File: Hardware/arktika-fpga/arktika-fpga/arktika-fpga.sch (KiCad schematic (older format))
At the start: 19 parts

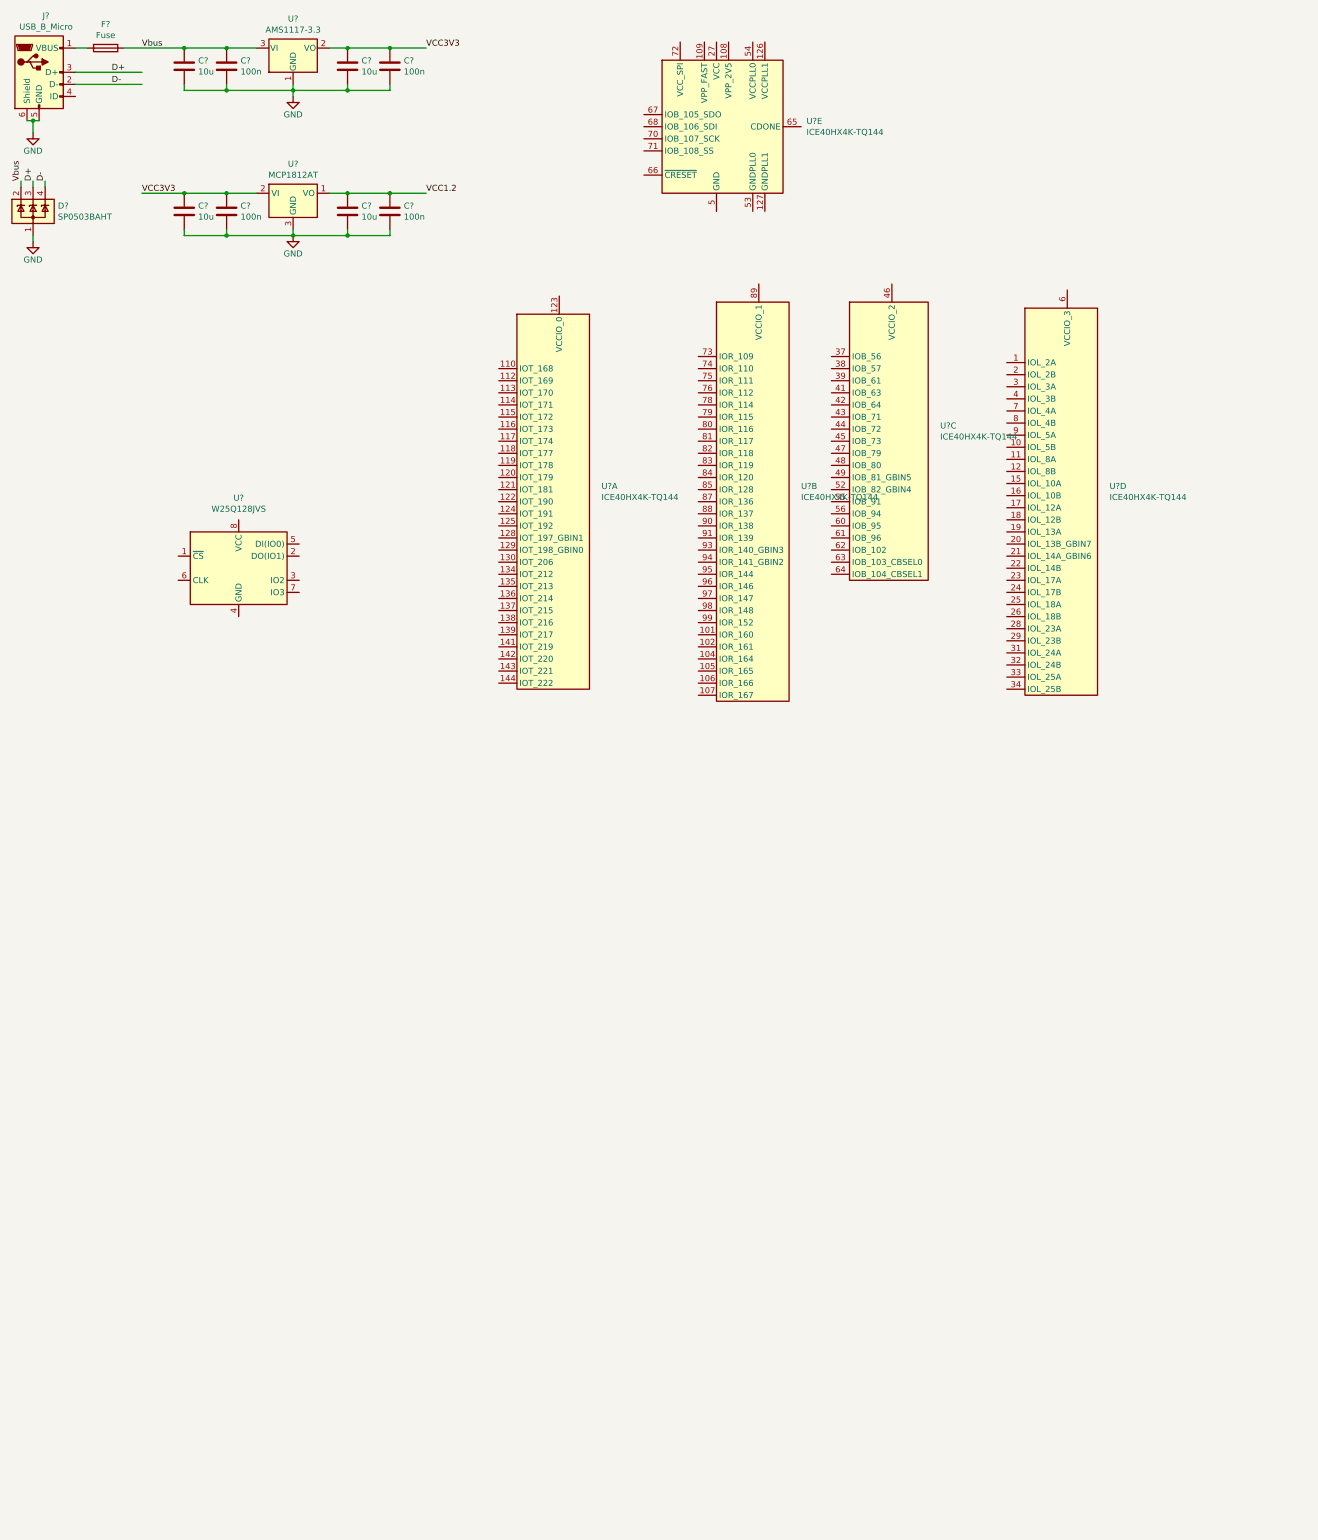
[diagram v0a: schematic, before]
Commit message: Added more docs do readme, did board power
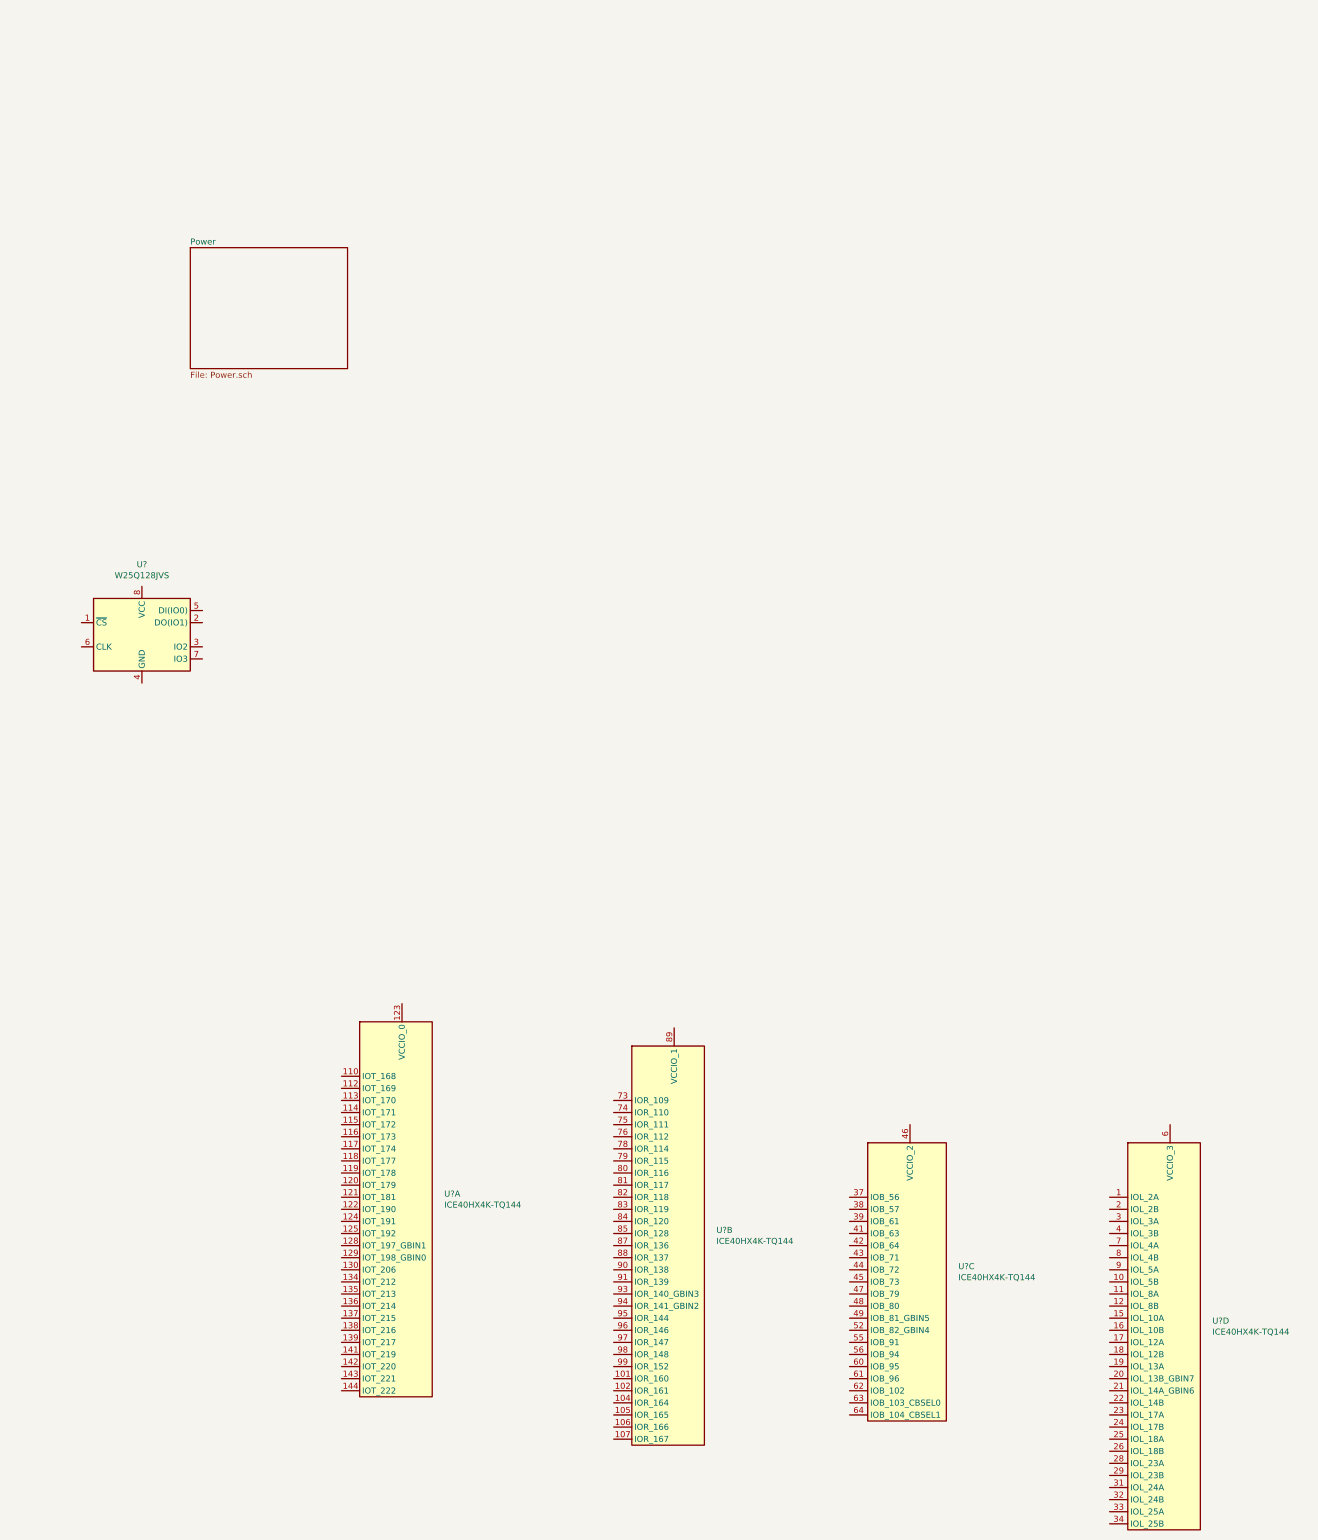
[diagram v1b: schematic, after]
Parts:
- removed C? (x4): 10u, symbol Device:C
- removed C? (x4): 100n, symbol Device:C
- removed D?: SP0503BAHT, Package_TO_SOT_SMD:SOT-143, symbol Power_Protection:SP0503BAHT
- removed F?: Fuse, symbol Device:Fuse
- removed J?: USB_B_Micro, symbol Connector:USB_B_Micro
- removed U?: MCP1812AT, TO_SOT_Packages_SMD:SOT-23, symbol Regulator_Linear:MCP1812AT
- removed U?: AMS1117-3.3, Package_TO_SOT_SMD:SOT-223-3_TabPin2, symbol Regulator_Linear:AMS1117-3.3
- removed U?: ICE40HX4K-TQ144, Package_QFP:TQFP-144_20x20mm_P0.5mm, symbol FPGA_Lattice:ICE40HX4K-TQ144
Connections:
- net labels removed: D+, D-, GND, VCC1.2, VCC3V3, Vbus
- wire segments 41 -> 0
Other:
- moved on the sheet: U?, U?A, U?B, U?C, U?D

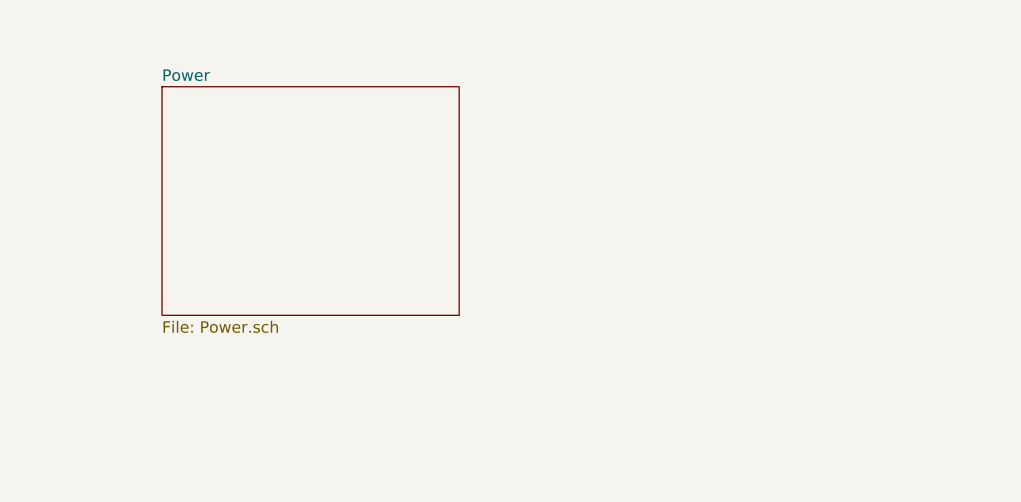
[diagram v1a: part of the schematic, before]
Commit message: Started doing usb and programming
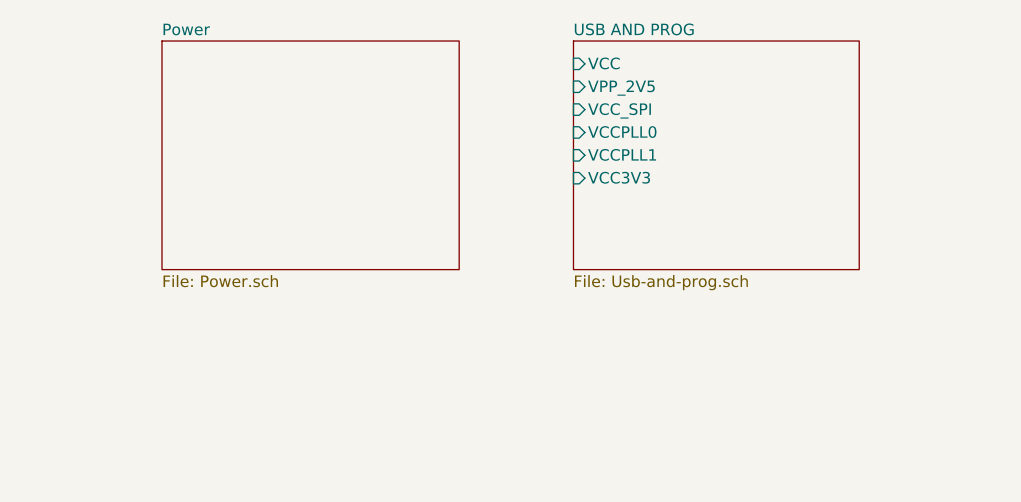
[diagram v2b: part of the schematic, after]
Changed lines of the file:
@@
 $Descr A4 11693 8268
 encoding utf-8
-Sheet 1 2
+Sheet 1 3
 Title "Arktika FPGA"
-Date "2020-07-25"
+Date "2020-07-26"
 Rev ""
 Comp "Author: Afonso Muralha"
@@
 $EndComp
 $Sheet
-S 2550 3300 1300 1000
+S 2550 3100 1300 1000
 U 5F3E98C5
 F0 "Power" 50
 F1 "Power.sch" 50
 $EndSheet
+$Sheet
+S 4350 3100 1250 1000
+U 5F415705
+F0 "USB AND PROG" 50
+F1 "Usb-and-prog.sch" 50
+F2 "VCC" I L 4350 3200 50
+F3 "VPP_2V5" I L 4350 3300 50
+F4 "VCC_SPI" I L 4350 3400 50
+F5 "VCCPLL0" I L 4350 3500 50
+F6 "VCCPLL1" I L 4350 3600 50
+F7 "VCC3V3" I L 4350 3700 50
+$EndSheet
 $EndSCHEMATC

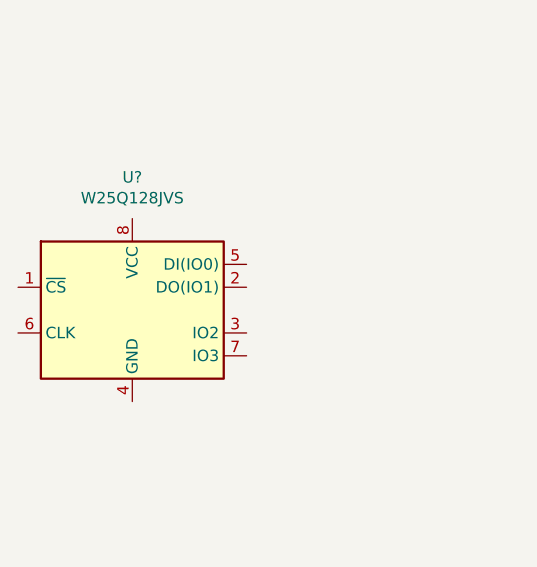
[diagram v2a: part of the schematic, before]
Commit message: Added misc components to the usb and prog schematic
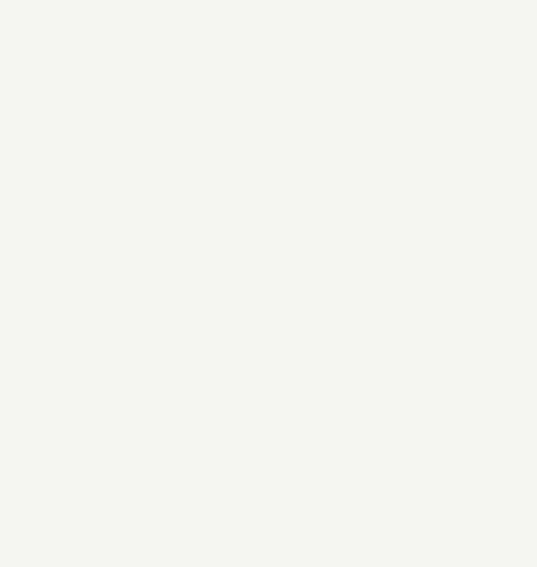
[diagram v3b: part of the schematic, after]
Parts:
- removed U?: W25Q128JVS, Package_SO:SOIC-8_5.23x5.23mm_P1.27mm, symbol Memory_Flash:W25Q128JVS
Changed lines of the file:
@@
-	1    0    0    -1
-$EndComp
-$Comp
-L Memory_Flash:W25Q128JVS U?
-U 1 1 5F1E5019
-P 2150 6500
-F 0 "U?" H 2150 7081 50  0000 C CNN
-F 1 "W25Q128JVS" H 2150 6990 50  0000 C CNN
-F 2 "Package_SO:SOIC-8_5.23x5.23mm_P1.27mm" H 2150 6500 50  0001 C CNN
-F 3 "http://www.winbond.com/resource-files/w25q128jv_dtr%20revc%2003272018%20plus.pdf" H 2150 6500 50  0001 C CNN
-	1    2150 6500
 	1    0    0    -1
 $EndComp
